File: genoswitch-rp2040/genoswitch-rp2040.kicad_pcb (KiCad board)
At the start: 2 copper layers, 43.4 x 57.3 mm, 44 parts, among them J1 USB_B_Micro, J10 RP2040_ADC2, J11 RP2040_ADC3, J2 Conn_01x03_Socket-PicoDebug, J3 HW-SPI0, J4 HW-SPI1, J5 PIO-SPI0, J6 PIO-SPI1, J7 SERIAL, J8 RP2040_ADC0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

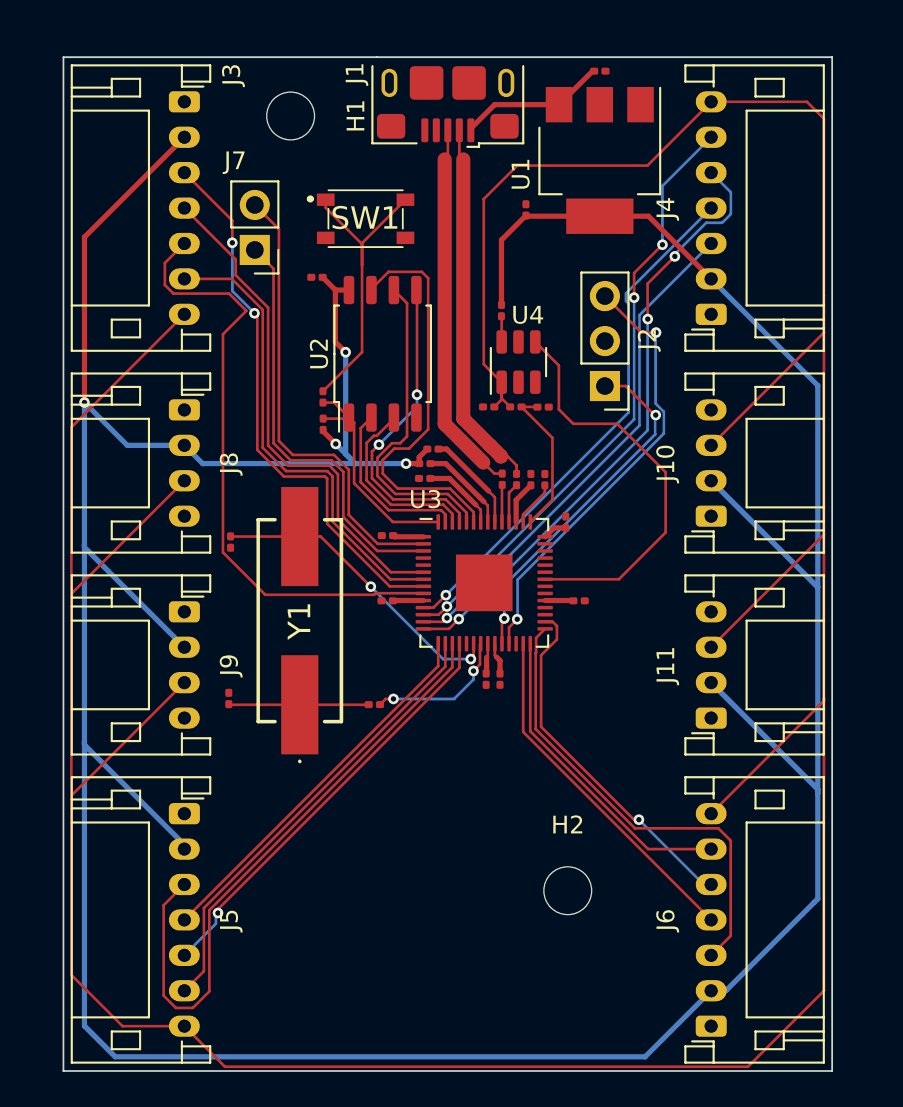
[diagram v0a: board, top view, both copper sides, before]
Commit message: (chore): Fix non-outline DRC errors
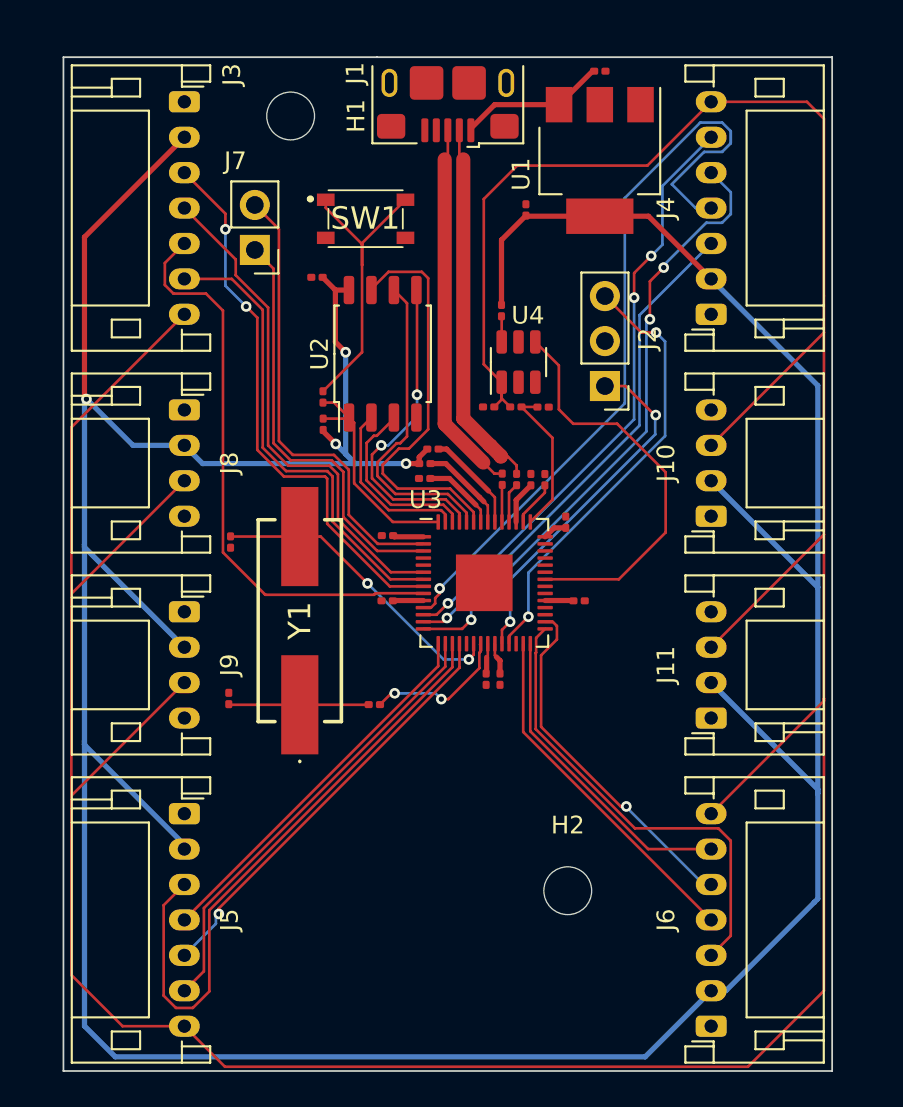
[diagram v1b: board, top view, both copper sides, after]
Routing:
- net /GPIO8: track 29.8 -> 43.8 mm
- net /GPIO7: track 34.6 -> 32.7 mm

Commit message: Re-trace board outline rails to adhere to new DRC rules
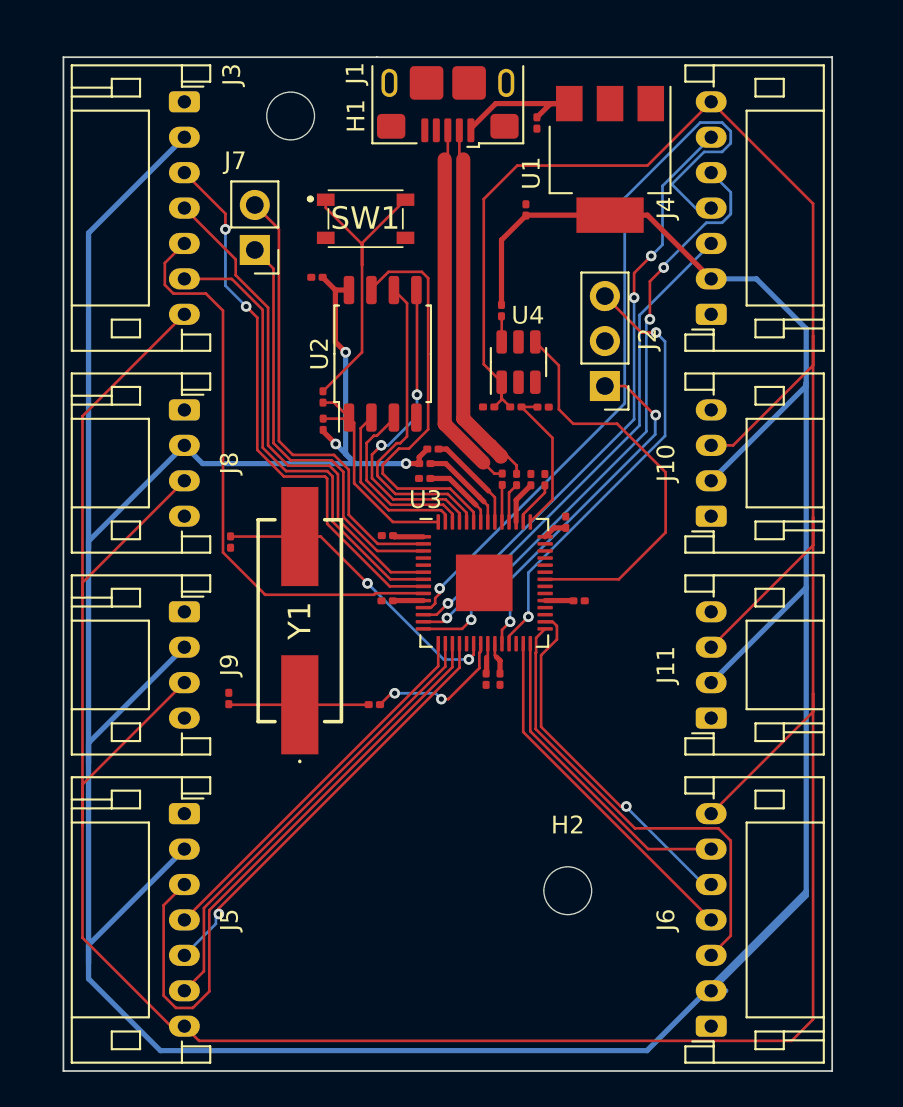
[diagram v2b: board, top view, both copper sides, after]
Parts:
- moved C1 4.60 mm to (112.3, 47.9), turned to -90 degrees
- moved U1 0.58 mm to (116.5, 50.0)
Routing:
- net +3V3: track 223.1 -> 230.6 mm, vias 4 -> 3
- net /ADC_VREF: track 219.4 -> 212.5 mm

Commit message: Shift J5, J6 by 90 degrees to make board slightly smaller
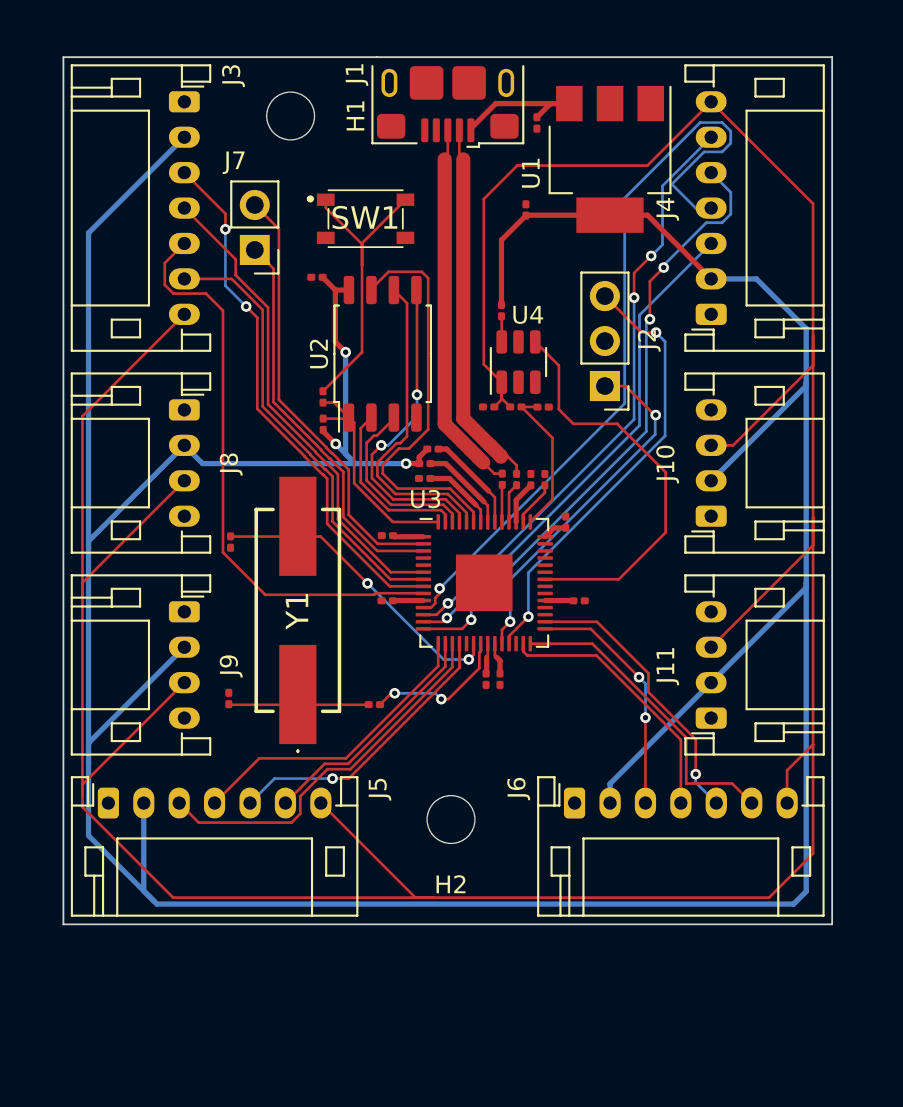
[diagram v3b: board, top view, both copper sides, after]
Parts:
- moved J6 14.8 mm to (114.5, 86.3), turned to 0 degrees
- moved H2 7.72 mm to (107.5, 87.3), turned to 180 degrees
- moved J5 4.33 mm to (88.1, 86.3), turned to 0 degrees
- moved Y1 0.59 mm to (98.8, 75.5)
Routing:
- net /ADC_VREF: track 212.5 -> 198.2 mm
- net +3V3: track 230.6 -> 216.6 mm
- net /GPIO14: track 35.3 -> 21.4 mm
- net /GPIO18: track 26.4 -> 13.7 mm, vias 0 -> 2
- net /GPIO13: track 25.7 -> 13.5 mm
- net /GPIO15: track 24.0 -> 16.3 mm
- net /GPIO16: track 20.0 -> 15.0 mm
- net /GPIO12: track 21.5 -> 17.1 mm
- net /GPIO19: track 20.1 -> 16.0 mm
- net Net-(J7-RX): track 23.8 -> 22.5 mm
- net /GPIO5: track 26.6 -> 25.2 mm
- net /GPIO6: track 31.4 -> 30.1 mm
- net /GPIO4: track 28.6 -> 27.2 mm
- net Net-(J7-TX): track 26.0 -> 24.6 mm
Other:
- board size 43.4 x 57.3 mm -> 43.4 x 49 mm

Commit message: Connect some power rails
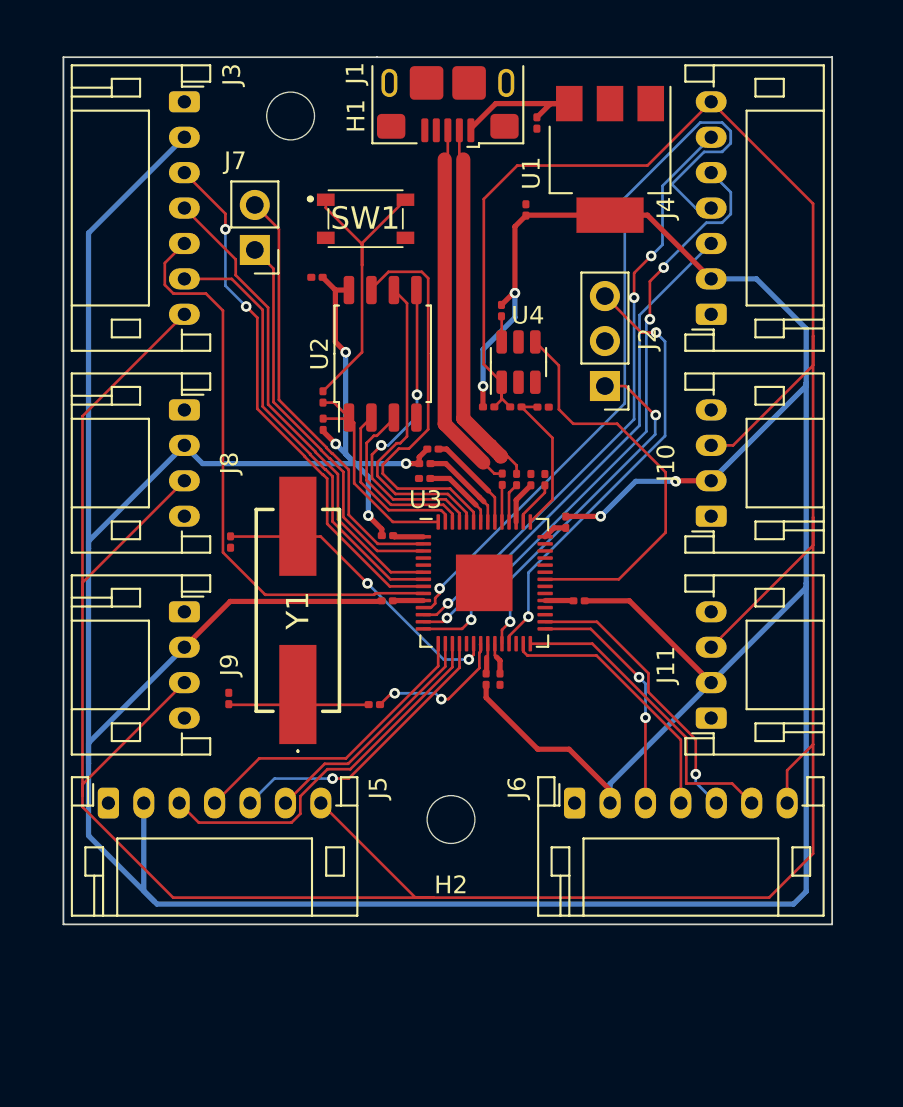
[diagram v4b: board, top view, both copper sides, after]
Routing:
- net +3V3: track 216.6 -> 269.7 mm, vias 3 -> 8
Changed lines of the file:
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@@
   (segment (start 98.93 80.8) (end 94.955 80.8) (width 0.1524) (layer "F.Cu") (net 4))
   (segment (start 94.955 80.8) (end 94.92 80.765) (width 0.1524) (layer "F.Cu") (net 4))
+  (segment (start 113.96 70.16) (end 113.95 70.17) (width 0.295656) (layer "F.Cu") (net 5))
+  (segment (start 103.562 70.882) (end 102.8 70.12) (width 0.295656) (layer "F.Cu") (net 5))
   (segment (start 111.725 53.15) (end 116.45 53.15) (width 0.295656) (layer "F.Cu") (net 5))
+  (segment (start 111.08 57.55) (end 110.99 57.55) (width 0.295656) (layer "F.Cu") (net 5))
+  (segment (start 112.37 83.31) (end 109.452 80.392) (width 0.295656) (layer "F.Cu") (net 5))
+  (segment (start 109.452 80.392) (end 109.452 79.675) (width 0.295656) (layer "F.Cu") (net 5))
+  (segment (start 103.562 71.247) (end 103.562 70.882) (width 0.295656) (layer "F.Cu") (net 5))
+  (segment (start 117.542 74.93) (end 115.022 74.93) (width 0.295656) (layer "F.Cu") (net 5))
+  (segment (start 111.08 53.795) (end 111.7 53.175) (width 0.295656) (layer "F.Cu") (net 5))
+  (segment (start 94.998372 74.963628) (end 92.412 77.55) (width 0.295656) (layer "F.Cu") (net 5))
+  (segment (start 116.45 86.35) (end 116.45 85.62) (width 0.295656) (layer "F.Cu") (net 5))
+  (segment (start 103.545 74.93) (end 103.511372 74.963628) (width 0.295656) (layer "F.Cu") (net 5))
   (segment (start 105.672 66.818) (end 105.672 67.18) (width 0.295656) (layer "F.Cu") (net 5))
+  (segment (start 122.162 79.55) (end 117.542 74.93) (width 0.295656) (layer "F.Cu") (net 5))
+  (segment (start 111.08 57.55) (end 111.08 53.795) (width 0.295656) (layer "F.Cu") (net 5))
   (segment (start 111.735 53.21) (end 111.7 53.175) (width 0.295656) (layer "F.Cu") (net 5))
-  (segment (start 110.32 54.555) (end 110.32 58.22) (width 0.295656) (layer "F.Cu") (net 5))
+  (segment (start 109.275 62.815) (end 109.28 62.81) (width 0.295656) (layer "F.Cu") (net 5))
   (segment (start 105.672 67.18) (end 104.93 67.18) (width 0.295656) (layer "F.Cu") (net 5))
+  (segment (start 115.92 70.16) (end 113.96 70.16) (width 0.295656) (layer "F.Cu") (net 5))
+  (segment (start 116.45 85.62) (end 114.14 83.31) (width 0.295656) (layer "F.Cu") (net 5))
+  (segment (start 103.511372 74.963628) (end 94.998372 74.963628) (width 0.295656) (layer "F.Cu") (net 5))
   (segment (start 101.705 57.38) (end 100.94 57.38) (width 0.295656) (layer "F.Cu") (net 5))
+  (segment (start 114.14 83.31) (end 112.37 83.31) (width 0.295656) (layer "F.Cu") (net 5))
+  (segment (start 109.275 63.98) (end 109.275 62.815) (width 0.295656) (layer "F.Cu") (net 5))
   (segment (start 100.25 65.36) (end 100.96 66.07) (width 0.295656) (layer "F.Cu") (net 5))
   (segment (start 100.94 57.38) (end 100.22 56.66) (width 0.295656) (layer "F.Cu") (net 5))
+  (segment (start 110.99 57.55) (end 110.32 58.22) (width 0.295656) (layer "F.Cu") (net 5))
   (segment (start 100.94 57.38) (end 100.94 60.31) (width 0.295656) (layer "F.Cu") (net 5))
   (segment (start 111.7 53.175) (end 111.725 53.15) (width 0.295656) (layer "F.Cu") (net 5))
   (segment (start 118.562 53.15) (end 116.45 53.15) (width 0.295656) (layer "F.Cu") (net 5))
+  (segment (start 120.19 68.15) (end 120.16 68.18) (width 0.295656) (layer "F.Cu") (net 5))
   (segment (start 100.94 60.31) (end 101.52 60.89) (width 0.295656) (layer "F.Cu") (net 5))
   (segment (start 122.162 56.75) (end 118.562 53.15) (width 0.295656) (layer "F.Cu") (net 5))
-  (segment (start 111.7 53.175) (end 110.32 54.555) (width 0.295656) (layer "F.Cu") (net 5))
+  (segment (start 122.162 68.15) (end 120.19 68.15) (width 0.295656) (layer "F.Cu") (net 5))
   (segment (start 106.13 66.36) (end 105.672 66.818) (width 0.295656) (layer "F.Cu") (net 5))
   (segment (start 100.25 65.28) (end 100.25 65.36) (width 0.295656) (layer "F.Cu") (net 5))
+  (via (at 111.08 57.55) (size 0.6) (drill 0.3) (layers "F.Cu" "B.Cu") (net 5))
+  (via (at 115.92 70.16) (size 0.6) (drill 0.3) (layers "F.Cu" "B.Cu") (net 5))
   (via (at 100.96 66.07) (size 0.6) (drill 0.3) (layers "F.Cu" "B.Cu") (net 5))
   (via (at 104.93 67.18) (size 0.6) (drill 0.3) (layers "F.Cu" "B.Cu") (net 5))
   (via (at 101.52 60.89) (size 0.6) (drill 0.3) (layers "F.Cu" "B.Cu") (net 5))
+  (via (at 120.16 68.18) (size 0.6) (drill 0.3) (layers "F.Cu" "B.Cu") (net 5))
+  (via (at 102.8 70.12) (size 0.6) (drill 0.3) (layers "F.Cu" "B.Cu") (net 5))
+  (via (at 109.28 62.81) (size 0.6) (drill 0.3) (layers "F.Cu" "B.Cu") (net 5))
   (segment (start 127.53 91.34) (end 126.817828 92.052172) (width 0.295656) (layer "B.Cu") (net 5))
   (segment (start 90.862172 92.052172) (end 90.705 91.895) (width 0.295656) (layer "B.Cu") (net 5))
@@
   (segment (start 104.93 67.18) (end 102.07 67.18) (width 0.295656) (layer "B.Cu") (net 5))
   (segment (start 127.53 62.61) (end 127.53 73.93) (width 0.295656) (layer "B.Cu") (net 5))
+  (segment (start 102.8 70.12) (end 102.8 67.91) (width 0.295656) (layer "B.Cu") (net 5))
+  (segment (start 109.28 60.73) (end 111.08 58.93) (width 0.295656) (layer "B.Cu") (net 5))
   (segment (start 87 84.12) (end 87 71.98) (width 0.295656) (layer "B.Cu") (net 5))
   (segment (start 87 71.562) (end 92.412 66.15) (width 0.295656) (layer "B.Cu") (net 5))
   (segment (start 122.162 56.75) (end 124.72 56.75) (width 0.295656) (layer "B.Cu") (net 5))
+  (segment (start 102.8 67.91) (end 101.845 66.955) (width 0.295656) (layer "B.Cu") (net 5))
   (segment (start 87 84.12) (end 87 82.962) (width 0.295656) (layer "B.Cu") (net 5))
   (segment (start 127.53 62.782) (end 122.162 68.15) (width 0.295656) (layer "B.Cu") (net 5))
   (segment (start 90.12 86.35) (end 90.12 91.31) (width 0.295656) (layer "B.Cu") (net 5))
   (segment (start 124.72 56.75) (end 127.53 59.56) (width 0.295656) (layer "B.Cu") (net 5))
+  (segment (start 117.9 68.18) (end 115.92 70.16) (width 0.295656) (layer "B.Cu") (net 5))
   (segment (start 90.705 91.895) (end 87 88.19) (width 0.295656) (layer "B.Cu") (net 5))
   (segment (start 87 88.19) (end 87 84.12) (width 0.295656) (layer "B.Cu") (net 5))
+  (segment (start 111.08 58.93) (end 111.08 57.55) (width 0.295656) (layer "B.Cu") (net 5))
   (segment (start 101.52 60.89) (end 101.52 66.63) (width 0.295656) (layer "B.Cu") (net 5))
   (segment (start 116.45 85.262) (end 122.162 79.55) (width 0.295656) (layer "B.Cu") (net 5))
@@
   (segment (start 127.53 59.56) (end 127.53 62.61) (width 0.295656) (layer "B.Cu") (net 5))
   (segment (start 116.45 86.35) (end 116.45 85.262) (width 0.295656) (layer "B.Cu") (net 5))
+  (segment (start 120.16 68.18) (end 117.9 68.18) (width 0.295656) (layer "B.Cu") (net 5))
   (segment (start 102.07 67.18) (end 93.442 67.18) (width 0.295656) (layer "B.Cu") (net 5))
   (segment (start 87 54.162) (end 92.412 48.75) (width 0.295656) (layer "B.Cu") (net 5))
   (segment (start 100.96 66.07) (end 101.845 66.955) (width 0.295656) (layer "B.Cu") (net 5))
+  (segment (start 109.28 62.81) (end 109.28 60.73) (width 0.295656) (layer "B.Cu") (net 5))
   (segment (start 127.53 74.182) (end 122.162 79.55) (width 0.295656) (layer "B.Cu") (net 5))
   (segment (start 107.382 68.02) (end 108.882 69.52) (width 0.295656) (layer "F.Cu") (net 6))
   (segment (start 110.236 78.304) (end 110.032 78.1) (width 0.295656) (layer "F.Cu") (net 6))
   (segment (start 110.236 79.034) (end 110.236 78.304) (width 0.295656) (layer "F.Cu") (net 6))
+  (segment (start 111.147 70.4765) (end 111.147 69.238) (width 0.295656) (layer "F.Cu") (net 6))
   (segment (start 109.947 77.3515) (end 109.947 78.015) (width 0.1524) (layer "F.Cu") (net 6))
   (segment (start 111.147 69.238) (end 111.98 68.405) (width 0.295656) (layer "F.Cu") (net 6))
@@
   (segment (start 106.302 68.02) (end 107.382 68.02) (width 0.295656) (layer "F.Cu") (net 6))
   (segment (start 109.947 78.015) (end 110.032 78.1) (width 0.1524) (layer "F.Cu") (net 6))
-  (segment (start 111.147 70.4765) (end 111.147 69.238) (width 0.295656) (layer "F.Cu") (net 6))
   (segment (start 111.547 70.045) (end 112.77 68.822) (width 0.1524) (layer "F.Cu") (net 7))
   (segment (start 111.547 70.4765) (end 111.547 70.045) (width 0.1524) (layer "F.Cu") (net 7))
